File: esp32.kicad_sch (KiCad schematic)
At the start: 17 parts

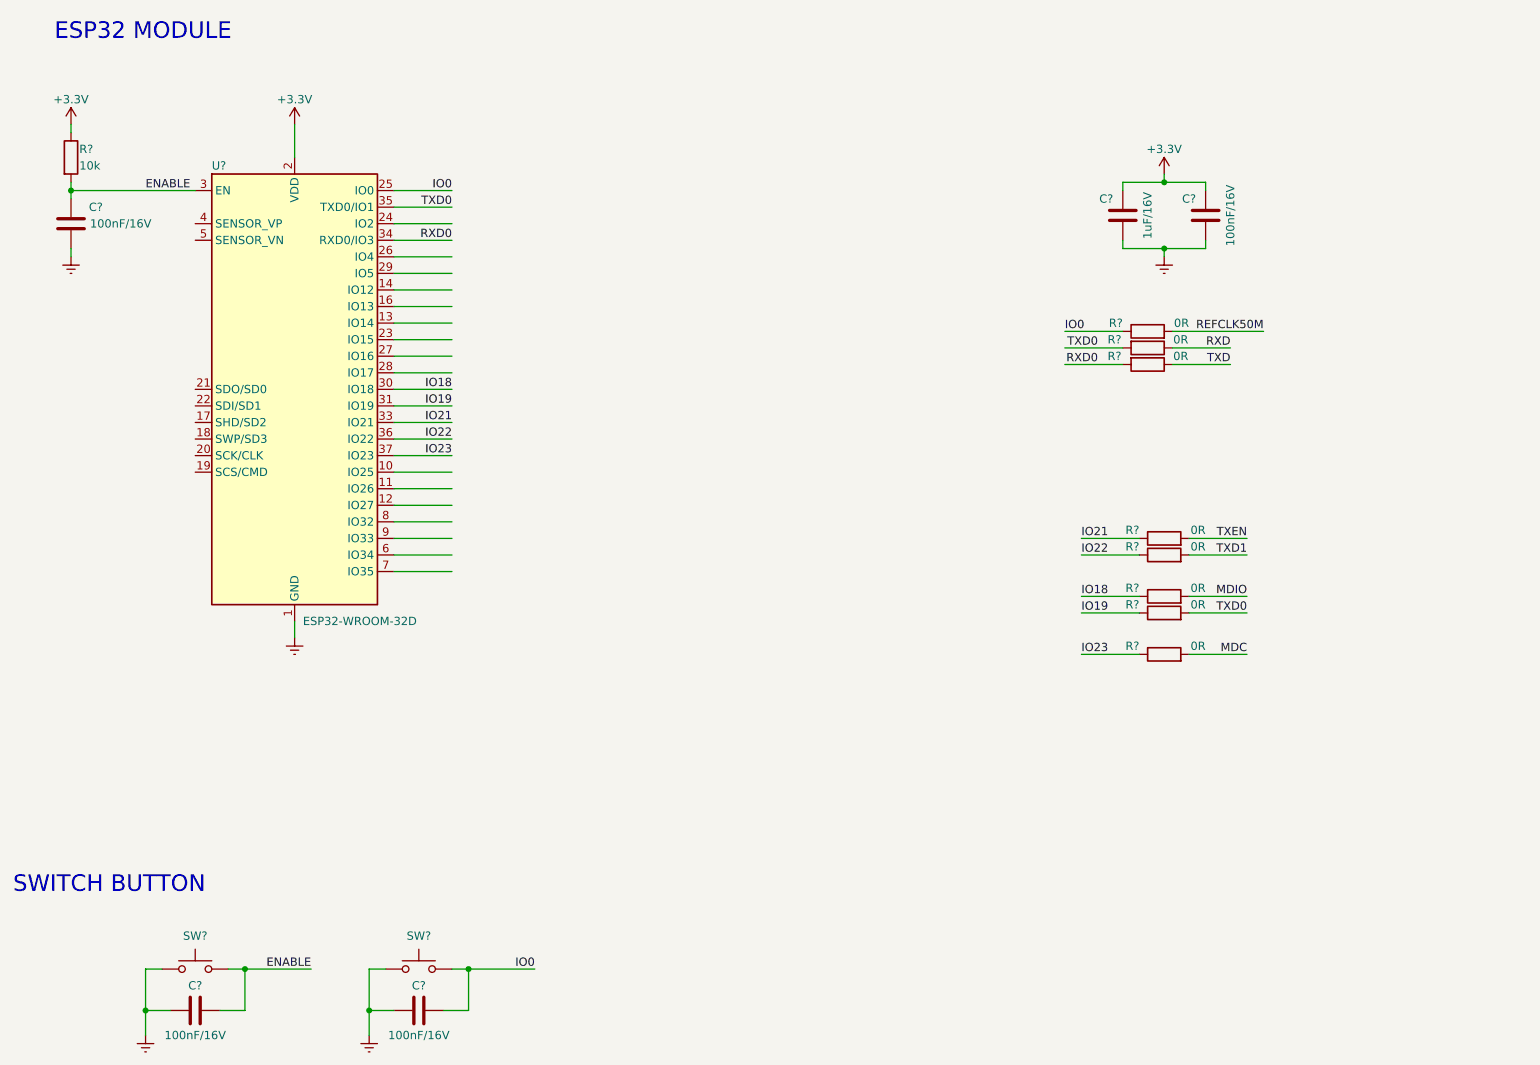
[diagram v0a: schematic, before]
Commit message: Adicionado o circuito de entrada do PHY ETH
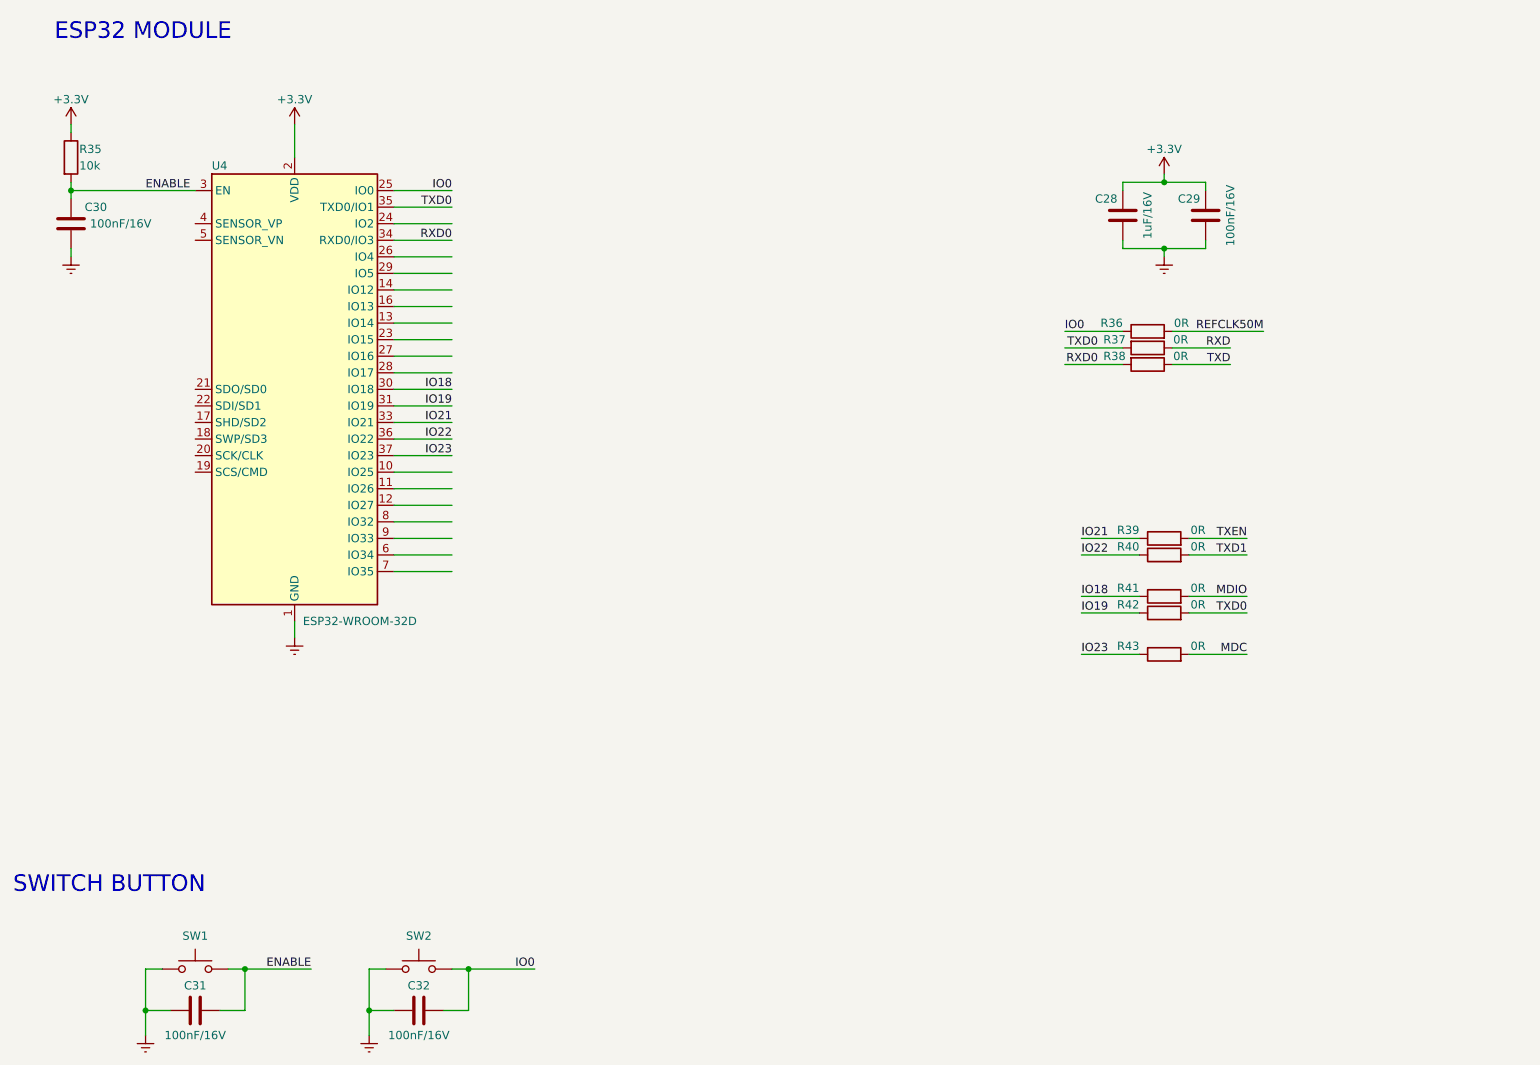
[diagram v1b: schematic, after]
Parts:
- gave numbers to parts that had none: 17
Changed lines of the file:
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@@
   (symbol (lib_id "Device:R") (at 50.8 46.99 0) (unit 1)
     (in_bom yes) (on_board yes)
-    (property "Reference" "R?" (id 0) (at 52.07 45.72 0)
+    (property "Reference" "R35" (id 0) (at 52.07 45.72 0)
       (effects (font (size 1.27 1.27)) (justify left))
     )
@@
   (symbol (lib_id "power:GNDREF") (at 62.23 181.61 0) (unit 1)
     (in_bom yes) (on_board yes) (fields_autoplaced)
-    (property "Reference" "#PWR?" (id 0) (at 62.23 187.96 0)
+    (property "Reference" "#PWR060" (id 0) (at 62.23 187.96 0)
       (effects (font (size 1.27 1.27)) hide)
     )
@@
   (symbol (lib_id "power:+3.3V") (at 50.8 41.91 0) (unit 1)
     (in_bom yes) (on_board yes)
-    (property "Reference" "#PWR?" (id 0) (at 50.8 45.72 0)
+    (property "Reference" "#PWR054" (id 0) (at 50.8 45.72 0)
       (effects (font (size 1.27 1.27)) hide)
     )
@@
   (symbol (lib_id "RF_Module:ESP32-WROOM-32D") (at 85.09 82.55 0) (unit 1)
     (in_bom yes) (on_board yes)
-    (property "Reference" "U?" (id 0) (at 72.39 48.26 0)
+    (property "Reference" "U4" (id 0) (at 72.39 48.26 0)
       (effects (font (size 1.27 1.27)) (justify left))
     )
@@
   (symbol (lib_id "Device:R") (at 218.44 107.95 90) (unit 1)
     (in_bom yes) (on_board yes)
-    (property "Reference" "R?" (id 0) (at 214.63 106.68 90)
+    (property "Reference" "R40" (id 0) (at 214.63 106.68 90)
       (effects (font (size 1.27 1.27)) (justify left))
     )
@@
   (symbol (lib_id "Device:C") (at 212.09 55.88 180) (unit 1)
     (in_bom yes) (on_board yes)
-    (property "Reference" "C?" (id 0) (at 209.55 53.34 0))
+    (property "Reference" "C28" (id 0) (at 209.55 53.34 0))
     (property "Value" "1uF/16V" (id 1) (at 215.9 55.88 90))
     (property "Footprint" "Capacitor_SMD:C_0603_1608Metric_Pad1.08x0.95mm_HandSolder" (id 2) (at 211.1248 52.07 0)
@@
   (symbol (lib_id "Device:R") (at 218.44 114.3 90) (unit 1)
     (in_bom yes) (on_board yes)
-    (property "Reference" "R?" (id 0) (at 214.63 113.03 90)
+    (property "Reference" "R41" (id 0) (at 214.63 113.03 90)
       (effects (font (size 1.27 1.27)) (justify left))
     )
@@
   (symbol (lib_id "Switch:SW_Push") (at 69.85 171.45 0) (unit 1)
     (in_bom yes) (on_board yes)
-    (property "Reference" "SW?" (id 0) (at 69.85 166.37 0))
+    (property "Reference" "SW1" (id 0) (at 69.85 166.37 0))
     (property "Value" "SW_Push" (id 1) (at 69.85 166.37 0)
       (effects (font (size 1.27 1.27)) hide)
@@
   (symbol (lib_id "power:+3.3V") (at 218.44 49.53 0) (unit 1)
     (in_bom yes) (on_board yes)
-    (property "Reference" "#PWR?" (id 0) (at 218.44 53.34 0)
+    (property "Reference" "#PWR056" (id 0) (at 218.44 53.34 0)
       (effects (font (size 1.27 1.27)) hide)
     )
@@
   (symbol (lib_id "Device:C") (at 69.85 177.8 270) (unit 1)
     (in_bom yes) (on_board yes)
-    (property "Reference" "C?" (id 0) (at 69.85 173.99 90))
+    (property "Reference" "C31" (id 0) (at 69.85 173.99 90))
     (property "Value" "100nF/16V" (id 1) (at 69.85 181.61 90))
     (property "Footprint" "Capacitor_SMD:C_0402_1005Metric_Pad0.74x0.62mm_HandSolder" (id 2) (at 66.04 178.7652 0)
@@
   (symbol (lib_id "Device:C") (at 104.14 177.8 270) (unit 1)
     (in_bom yes) (on_board yes)
-    (property "Reference" "C?" (id 0) (at 104.14 173.99 90))
+    (property "Reference" "C32" (id 0) (at 104.14 173.99 90))
     (property "Value" "100nF/16V" (id 1) (at 104.14 181.61 90))
     (property "Footprint" "Capacitor_SMD:C_0402_1005Metric_Pad0.74x0.62mm_HandSolder" (id 2) (at 100.33 178.7652 0)
@@
   (symbol (lib_id "Device:R") (at 215.9 76.2 270) (unit 1)
     (in_bom yes) (on_board yes)
-    (property "Reference" "R?" (id 0) (at 210.82 74.93 90))
+    (property "Reference" "R37" (id 0) (at 210.82 74.93 90))
     (property "Value" "0R" (id 1) (at 220.98 74.93 90))
     (property "Footprint" "Resistor_SMD:R_0402_1005Metric_Pad0.72x0.64mm_HandSolder" (id 2) (at 215.9 74.422 90)
@@
   (symbol (lib_id "power:GNDREF") (at 96.52 181.61 0) (unit 1)
     (in_bom yes) (on_board yes) (fields_autoplaced)
-    (property "Reference" "#PWR?" (id 0) (at 96.52 187.96 0)
+    (property "Reference" "#PWR061" (id 0) (at 96.52 187.96 0)
       (effects (font (size 1.27 1.27)) hide)
     )
@@
   (symbol (lib_id "Switch:SW_Push") (at 104.14 171.45 0) (unit 1)
     (in_bom yes) (on_board yes)
-    (property "Reference" "SW?" (id 0) (at 104.14 166.37 0))
+    (property "Reference" "SW2" (id 0) (at 104.14 166.37 0))
     (property "Value" "SW_Push" (id 1) (at 104.14 166.37 0)
       (effects (font (size 1.27 1.27)) hide)
@@
   (symbol (lib_id "power:GNDREF") (at 50.8 62.23 0) (unit 1)
     (in_bom yes) (on_board yes) (fields_autoplaced)
-    (property "Reference" "#PWR?" (id 0) (at 50.8 68.58 0)
+    (property "Reference" "#PWR057" (id 0) (at 50.8 68.58 0)
       (effects (font (size 1.27 1.27)) hide)
     )
@@
   (symbol (lib_id "Device:R") (at 218.44 123.19 90) (unit 1)
     (in_bom yes) (on_board yes)
-    (property "Reference" "R?" (id 0) (at 214.63 121.92 90)
+    (property "Reference" "R43" (id 0) (at 214.63 121.92 90)
       (effects (font (size 1.27 1.27)) (justify left))
     )
@@
   (symbol (lib_id "Device:R") (at 215.9 78.74 270) (unit 1)
     (in_bom yes) (on_board yes)
-    (property "Reference" "R?" (id 0) (at 210.82 77.47 90))
+    (property "Reference" "R38" (id 0) (at 210.82 77.47 90))
     (property "Value" "0R" (id 1) (at 220.98 77.47 90))
     (property "Footprint" "Resistor_SMD:R_0402_1005Metric_Pad0.72x0.64mm_HandSolder" (id 2) (at 215.9 76.962 90)
@@
   (symbol (lib_id "power:GNDREF") (at 218.44 62.23 0) (unit 1)
     (in_bom yes) (on_board yes) (fields_autoplaced)
-    (property "Reference" "#PWR?" (id 0) (at 218.44 68.58 0)
+    (property "Reference" "#PWR058" (id 0) (at 218.44 68.58 0)
       (effects (font (size 1.27 1.27)) hide)
     )
@@
   (symbol (lib_id "Device:C") (at 224.79 55.88 180) (unit 1)
     (in_bom yes) (on_board yes)
-    (property "Reference" "C?" (id 0) (at 222.25 53.34 0))
+    (property "Reference" "C29" (id 0) (at 222.25 53.34 0))
     (property "Value" "100nF/16V" (id 1) (at 228.6 55.88 90))
     (property "Footprint" "Capacitor_SMD:C_0402_1005Metric_Pad0.74x0.62mm_HandSolder" (id 2) (at 223.8248 52.07 0)
@@
   (symbol (lib_id "Device:R") (at 218.44 105.41 90) (unit 1)
     (in_bom yes) (on_board yes)
-    (property "Reference" "R?" (id 0) (at 214.63 104.14 90)
+    (property "Reference" "R39" (id 0) (at 214.63 104.14 90)
       (effects (font (size 1.27 1.27)) (justify left))
     )
@@
   (symbol (lib_id "power:+3.3V") (at 85.09 41.91 0) (unit 1)
     (in_bom yes) (on_board yes)
-    (property "Reference" "#PWR?" (id 0) (at 85.09 45.72 0)
+    (property "Reference" "#PWR055" (id 0) (at 85.09 45.72 0)
       (effects (font (size 1.27 1.27)) hide)
     )
@@
   (symbol (lib_id "Device:R") (at 218.44 116.84 90) (unit 1)
     (in_bom yes) (on_board yes)
-    (property "Reference" "R?" (id 0) (at 214.63 115.57 90)
+    (property "Reference" "R42" (id 0) (at 214.63 115.57 90)
       (effects (font (size 1.27 1.27)) (justify left))
     )
@@
   (symbol (lib_id "power:GNDREF") (at 85.09 120.65 0) (unit 1)
     (in_bom yes) (on_board yes) (fields_autoplaced)
-    (property "Reference" "#PWR?" (id 0) (at 85.09 127 0)
+    (property "Reference" "#PWR059" (id 0) (at 85.09 127 0)
       (effects (font (size 1.27 1.27)) hide)
     )
@@
   (symbol (lib_id "Device:R") (at 215.9 73.66 90) (unit 1)
     (in_bom yes) (on_board yes)
-    (property "Reference" "R?" (id 0) (at 212.09 72.39 90)
+    (property "Reference" "R36" (id 0) (at 212.09 72.39 90)
       (effects (font (size 1.27 1.27)) (justify left))
     )
@@
   (symbol (lib_id "Device:C") (at 50.8 57.15 180) (unit 1)
     (in_bom yes) (on_board yes)
-    (property "Reference" "C?" (id 0) (at 54.61 54.61 0))
+    (property "Reference" "C30" (id 0) (at 54.61 54.61 0))
     (property "Value" "100nF/16V" (id 1) (at 58.42 57.15 0))
     (property "Footprint" "Capacitor_SMD:C_0402_1005Metric_Pad0.74x0.62mm_HandSolder" (id 2) (at 49.8348 53.34 0)

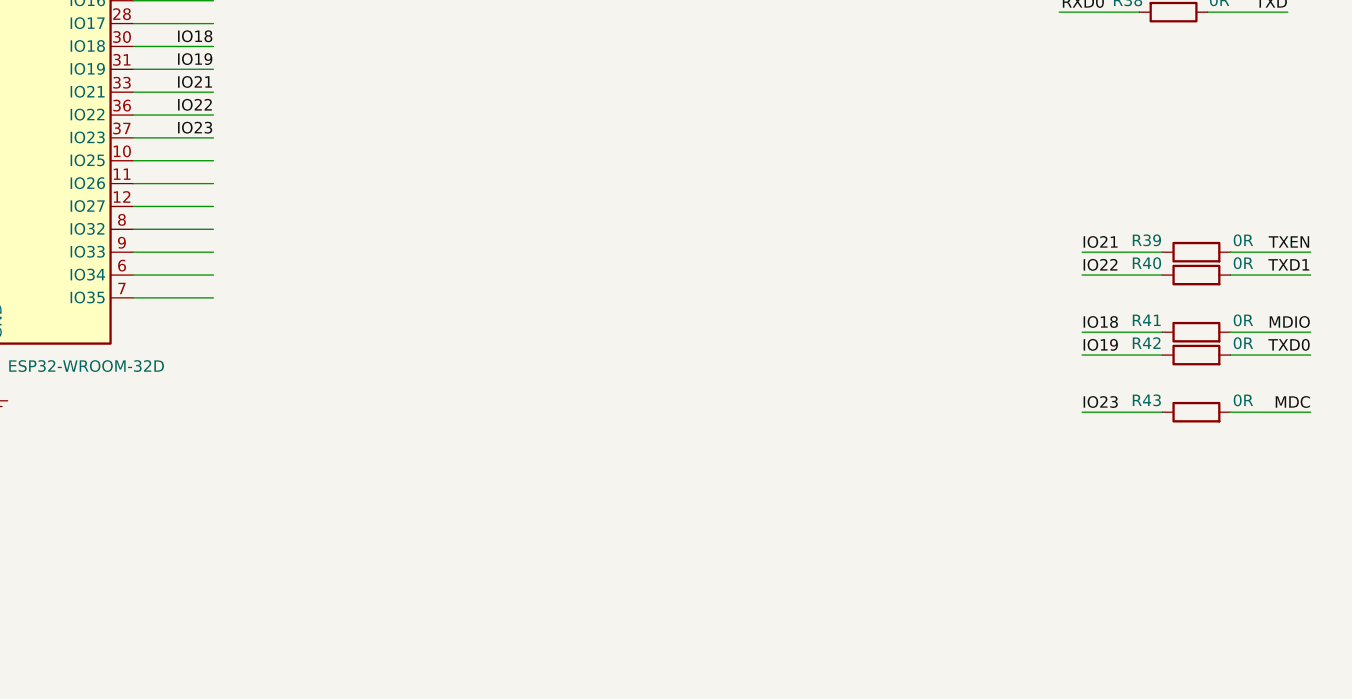
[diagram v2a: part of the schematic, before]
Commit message: Circuito de Reset e Serial TxD do módulo BG95
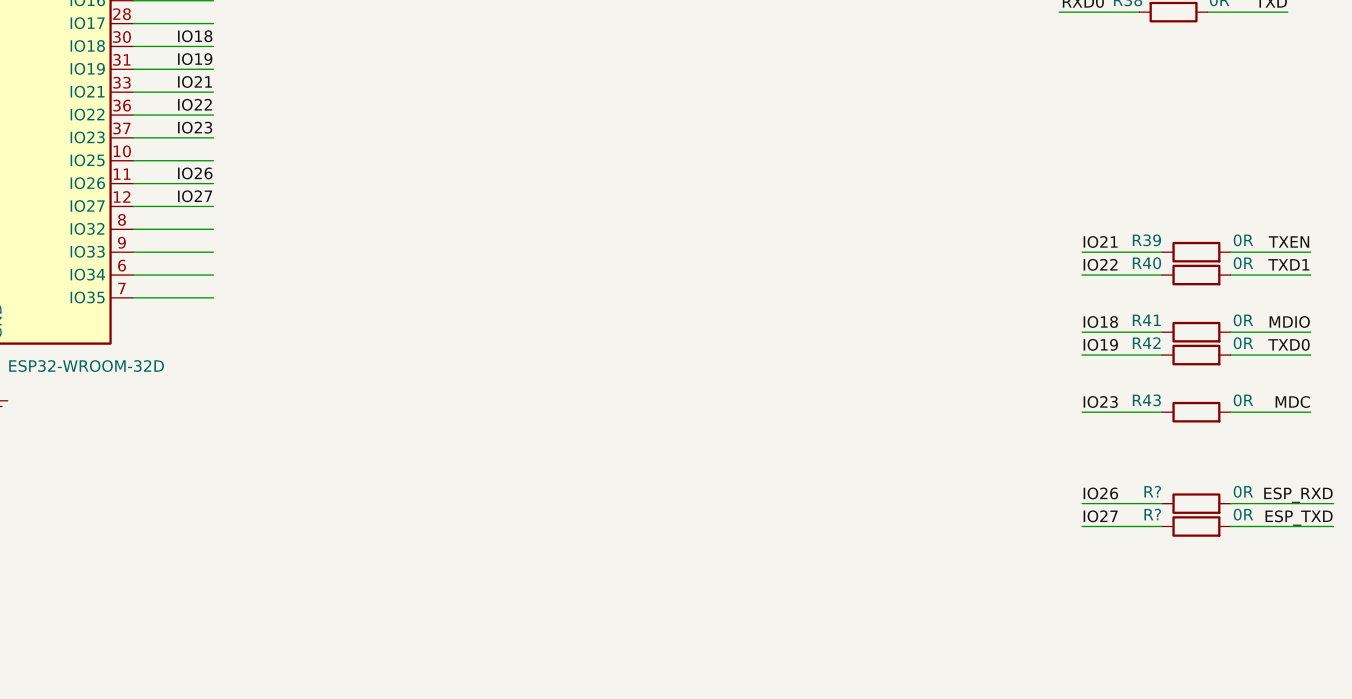
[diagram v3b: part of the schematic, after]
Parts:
- added R? (x2): 0R, Resistor_SMD:R_0402_1005Metric_Pad0.72x0.64mm_HandSolder, symbol Device:R
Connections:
- net IO26: now reaches U4.11 (IO26)
- net IO26: now also R?.1
- net IO27: now reaches U4.12 (IO27)
- net IO27: now also R?.1
- new net ESP_RXD: R?.2
- new net ESP_TXD: R?.2
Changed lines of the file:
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@@
+    (stroke (width 0) (type default) (color 0 0 0 0))
+  )
+  (wire (pts (xy 205.74 135.89) (xy 214.63 135.89))
     (stroke (width 0) (type default) (color 0 0 0 0))
   )
@@
     (stroke (width 0) (type default) (color 0 0 0 0))
   )
+  (wire (pts (xy 222.25 135.89) (xy 233.68 135.89))
+    (stroke (width 0) (type default) (color 0 0 0 0))
+  )
+  (wire (pts (xy 205.74 133.35) (xy 214.63 133.35))
+    (stroke (width 0) (type default) (color 0 0 0 0))
+  )
   (wire (pts (xy 100.33 74.93) (xy 109.22 74.93))
     (stroke (width 0) (type default) (color 0 0 0 0))
@@
   )
   (wire (pts (xy 100.33 97.79) (xy 109.22 97.79))
+    (stroke (width 0) (type default) (color 0 0 0 0))
+  )
+  (wire (pts (xy 222.25 133.35) (xy 233.68 133.35))
     (stroke (width 0) (type default) (color 0 0 0 0))
   )
@@
     (effects (font (size 1.27 1.27)) (justify left bottom))
   )
+  (label "IO27" (at 109.22 100.33 180)
+    (effects (font (size 1.27 1.27)) (justify right bottom))
+  )
   (label "IO23" (at 205.74 123.19 0)
     (effects (font (size 1.27 1.27)) (justify left bottom))
@@
     (effects (font (size 1.27 1.27)) (justify right bottom))
   )
+  (label "ESP_TXD" (at 233.68 135.89 180)
+    (effects (font (size 1.27 1.27)) (justify right bottom))
+  )
   (label "IO0" (at 109.22 52.07 180)
     (effects (font (size 1.27 1.27)) (justify right bottom))
@@
     (effects (font (size 1.27 1.27)) (justify left bottom))
   )
+  (label "IO26" (at 205.74 133.35 0)
+    (effects (font (size 1.27 1.27)) (justify left bottom))
+  )
   (label "RXD0" (at 208.28 78.74 180)
     (effects (font (size 1.27 1.27)) (justify right bottom))
@@
     (effects (font (size 1.27 1.27)) (justify right bottom))
   )
+  (label "IO26" (at 109.22 97.79 180)
+    (effects (font (size 1.27 1.27)) (justify right bottom))
+  )
   (label "MDC" (at 231.14 123.19 180)
     (effects (font (size 1.27 1.27)) (justify right bottom))
@@
   (label "IO19" (at 109.22 85.09 180)
     (effects (font (size 1.27 1.27)) (justify right bottom))
+  )
+  (label "ESP_RXD" (at 233.68 133.35 180)
+    (effects (font (size 1.27 1.27)) (justify right bottom))
+  )
+  (label "IO27" (at 205.74 135.89 0)
+    (effects (font (size 1.27 1.27)) (justify left bottom))
   )
   (label "TXD0" (at 208.28 76.2 180)
@@
     (pin "1")
   )
+  (symbol (lib_id "Device:R") (at 218.44 133.35 90) (unit 1)
+    (in_bom yes) (on_board yes)
+    (property "Reference" "R?" (id 0) (at 214.63 132.08 90)
+      (effects (font (size 1.27 1.27)) (justify left))
+    )
+    (property "Value" "0R" (id 1) (at 224.79 132.08 90)
+      (effects (font (size 1.27 1.27)) (justify left))
+    )
+    (property "Footprint" "Resistor_SMD:R_0402_1005Metric_Pad0.72x0.64mm_HandSolder" (id 2) (at 218.44 135.128 90)
+      (effects (font (size 1.27 1.27)) hide)
+    )
+    (property "Datasheet" "~" (id 3) (at 218.44 133.35 0)
+      (effects (font (size 1.27 1.27)) hide)
+    )
+    (pin "1")
+    (pin "2")
+  )
   (symbol (lib_id "Device:R") (at 218.44 123.19 90) (unit 1)
     (in_bom yes) (on_board yes)
@@
     (pin "1")
   )
+  (symbol (lib_id "Device:R") (at 218.44 135.89 90) (unit 1)
+    (in_bom yes) (on_board yes)
+    (property "Reference" "R?" (id 0) (at 214.63 134.62 90)
+      (effects (font (size 1.27 1.27)) (justify left))
+    )
+    (property "Value" "0R" (id 1) (at 224.79 134.62 90)
+      (effects (font (size 1.27 1.27)) (justify left))
+    )
+    (property "Footprint" "Resistor_SMD:R_0402_1005Metric_Pad0.72x0.64mm_HandSolder" (id 2) (at 218.44 137.668 90)
+      (effects (font (size 1.27 1.27)) hide)
+    )
+    (property "Datasheet" "~" (id 3) (at 218.44 135.89 0)
+      (effects (font (size 1.27 1.27)) hide)
+    )
+    (pin "1")
+    (pin "2")
+  )
   (symbol (lib_id "Device:R") (at 218.44 116.84 90) (unit 1)
